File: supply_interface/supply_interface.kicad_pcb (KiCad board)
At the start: 2 copper layers, 93 x 152 mm, 66 parts, among them J1 39-28-1243, J10 MBES-152, J12 MBES-152, J13 MBES-152, J14 39-28-1043, J15 3-641215-2, J2 39-28-1063, J4 MBES-152, J5 282837-3, J6 MBES-152, J7 39-28-1083, J8 MBES-152, J9 MBES-152

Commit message: Update J14
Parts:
- F7: value SF-1206S1000R-2 -> 10 A S.B
- J14: value 39-28-1043 -> 39-30-1041; footprint vq:39-28-1043 -> vq:39-30-104Y
- moved C23 14.8 mm to (102.2, 74.9), turned to 180 degrees
- moved D5 12.2 mm to (103.2, 78.6), turned to 180 degrees
- moved C21 12.1 mm to (103.9, 82.4), turned to 0 degrees
- moved C22 11.3 mm to (103.9, 80.7), turned to 0 degrees
- moved F7 8.92 mm to (107.6, 83.9), turned to 90 degrees
- moved J14 5.06 mm to (117.5, 74.2), turned to 90 degrees
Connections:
- J14 pad 1: /pc -> GND
- J14 pad 2: /pc -> GND
- J14 pad 3: GND -> /pc
- J14 pad 4: GND -> /pc

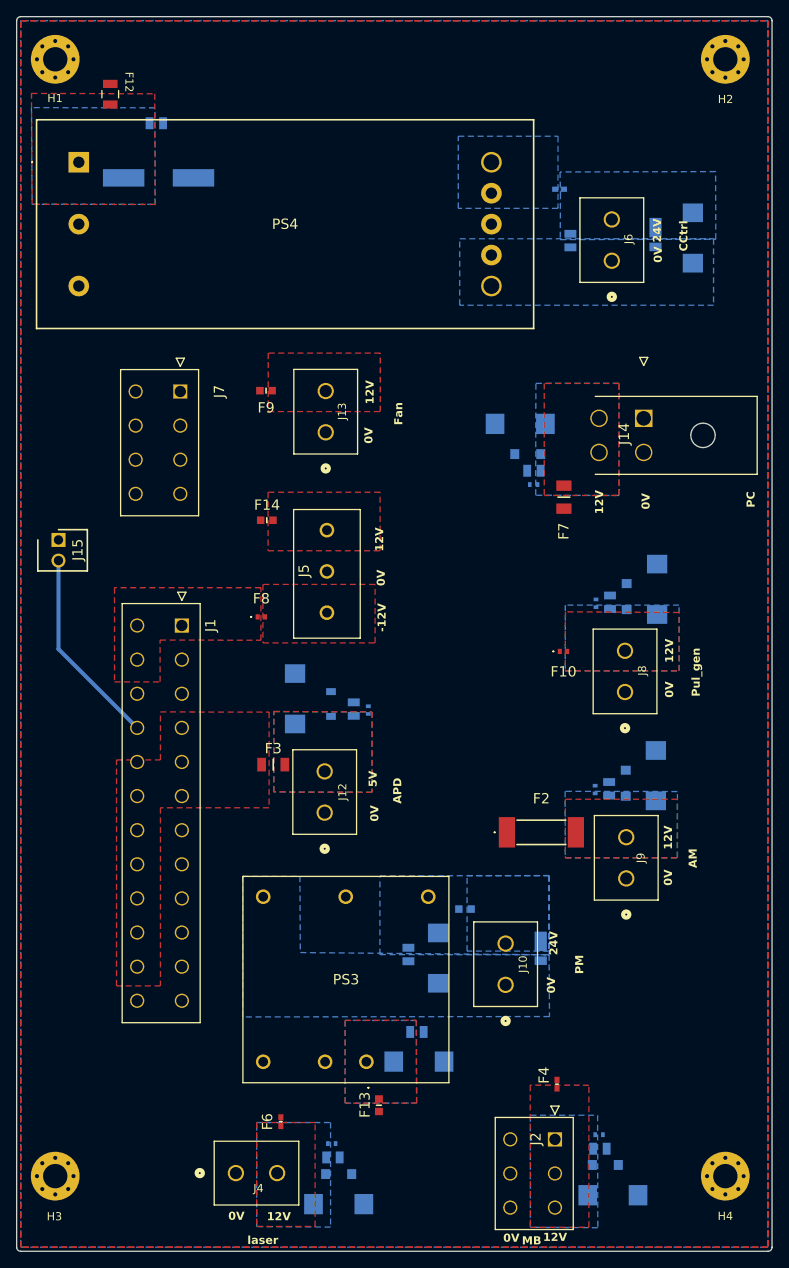
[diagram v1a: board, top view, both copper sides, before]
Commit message: Update board_shape
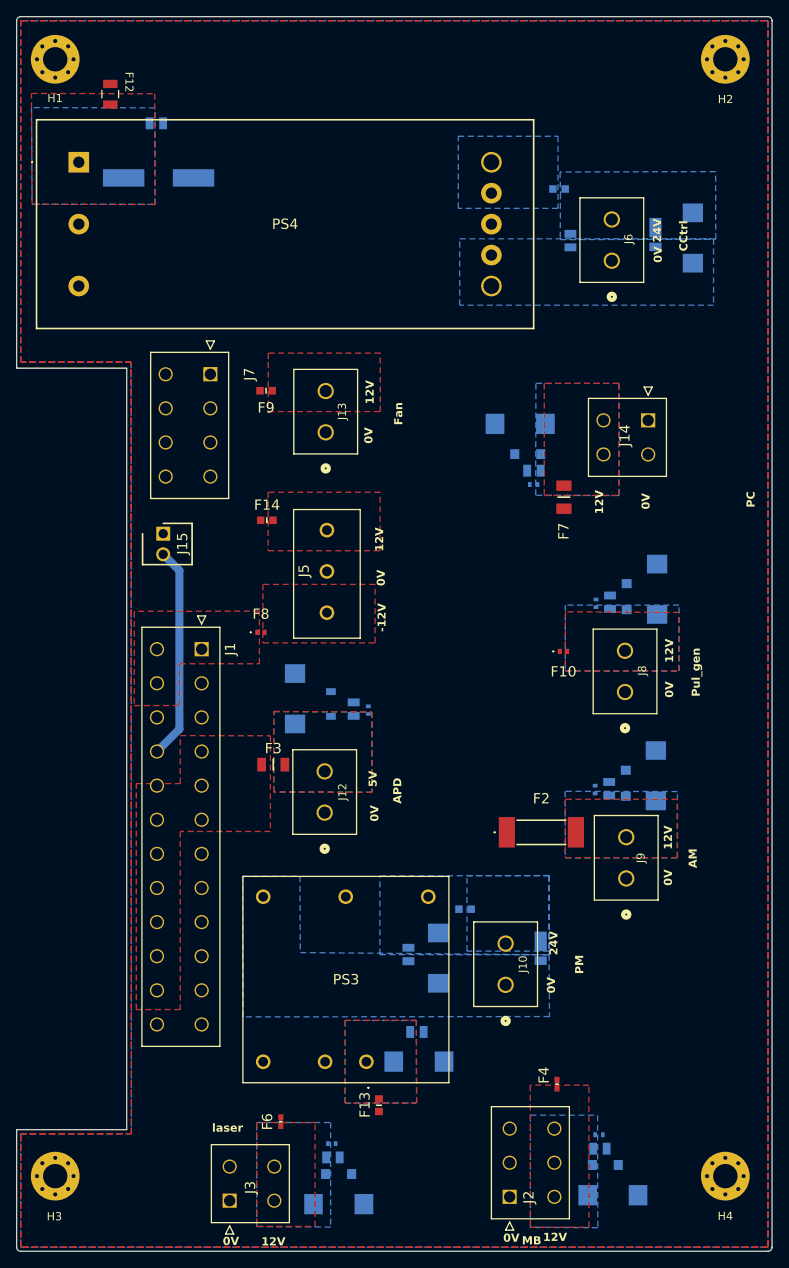
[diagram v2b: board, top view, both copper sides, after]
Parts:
- removed J4: MBES-152, vq:CONN_MBES-152_ALT
- added J3: 39-28-1043, vq:39-28-1043, F.Cu at (66.5, 170.5)
- F5: footprint vq:FUSC1005X61N -> vq:FUSC1608X55N
- J14: value 39-30-1041 -> 39-28-1043; footprint vq:39-30-104Y -> vq:39-28-1043
- moved J15 12.9 mm to (58.3, 88.4)
- moved J2 9.01 mm to (101.0, 170.1), turned to 90 degrees
- moved J7 4.27 mm to (64.1, 68.8)
- moved J1 3.80 mm to (63.0, 102.6)
- moved F8 1.90 mm to (70.3, 100.5)
- moved J14 0.60 mm to (118.0, 74.5), turned to -90 degrees
- moved F5 0.07 mm to (107.0, 46.0)
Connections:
- J2 pad 1: /MB -> GND
- J2 pad 2: /MB -> GND
- J2 pad 3: /MB -> GND
- J2 pad 4: GND -> /MB
- J2 pad 5: GND -> /MB
- J2 pad 6: GND -> /MB
- J7 pad 1: 12V -> GND
- J7 pad 2: 12V -> GND
- J7 pad 3: 12V -> GND
- J7 pad 4: 12V -> GND
- J7 pad 5: GND -> 12V
- J7 pad 6: GND -> 12V
- J7 pad 7: GND -> 12V
- J7 pad 8: GND -> 12V
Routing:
- net Net-(J1-Pad16): track 24.6 -> 26.2 mm
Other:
- outline, holes or cut-outs redrawn
